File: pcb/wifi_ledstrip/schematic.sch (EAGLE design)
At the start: 64 parts, among them IC1 STM32F10XCXT6, Q1 8MHz

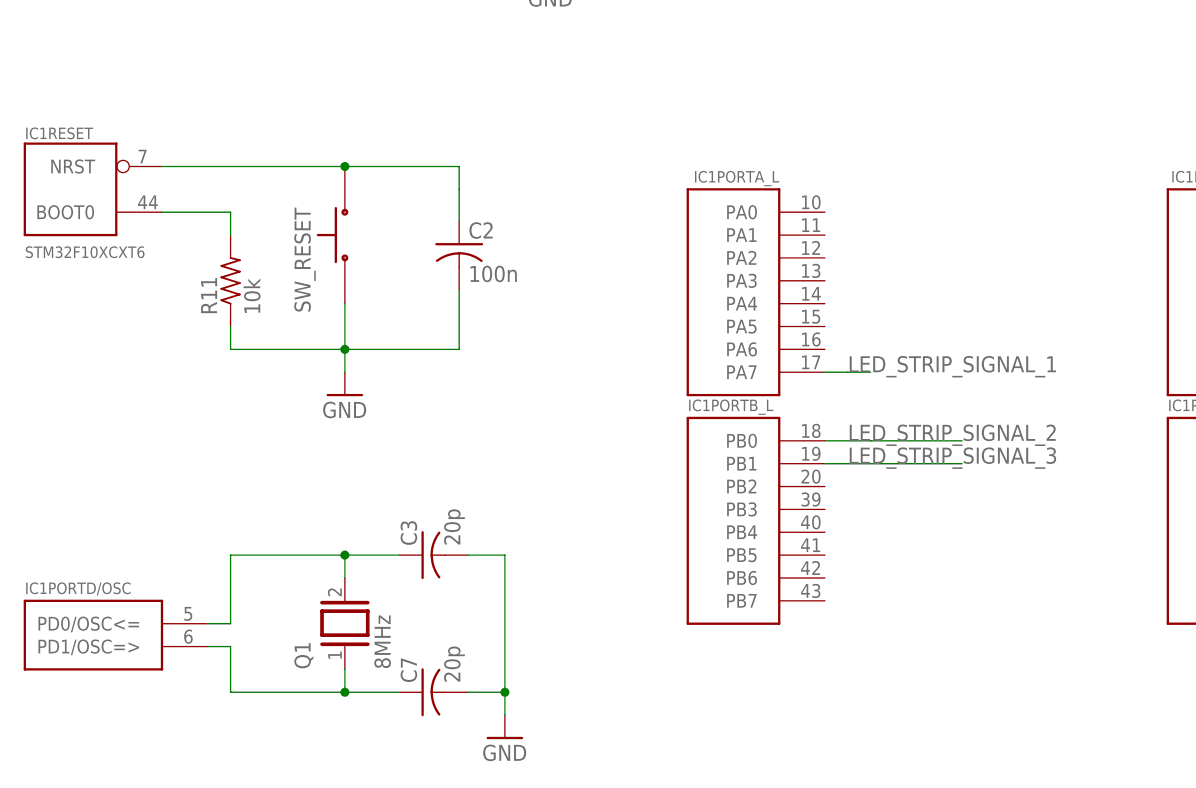
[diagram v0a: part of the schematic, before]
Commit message: pcb fix - boot1 pin pulled to gnd
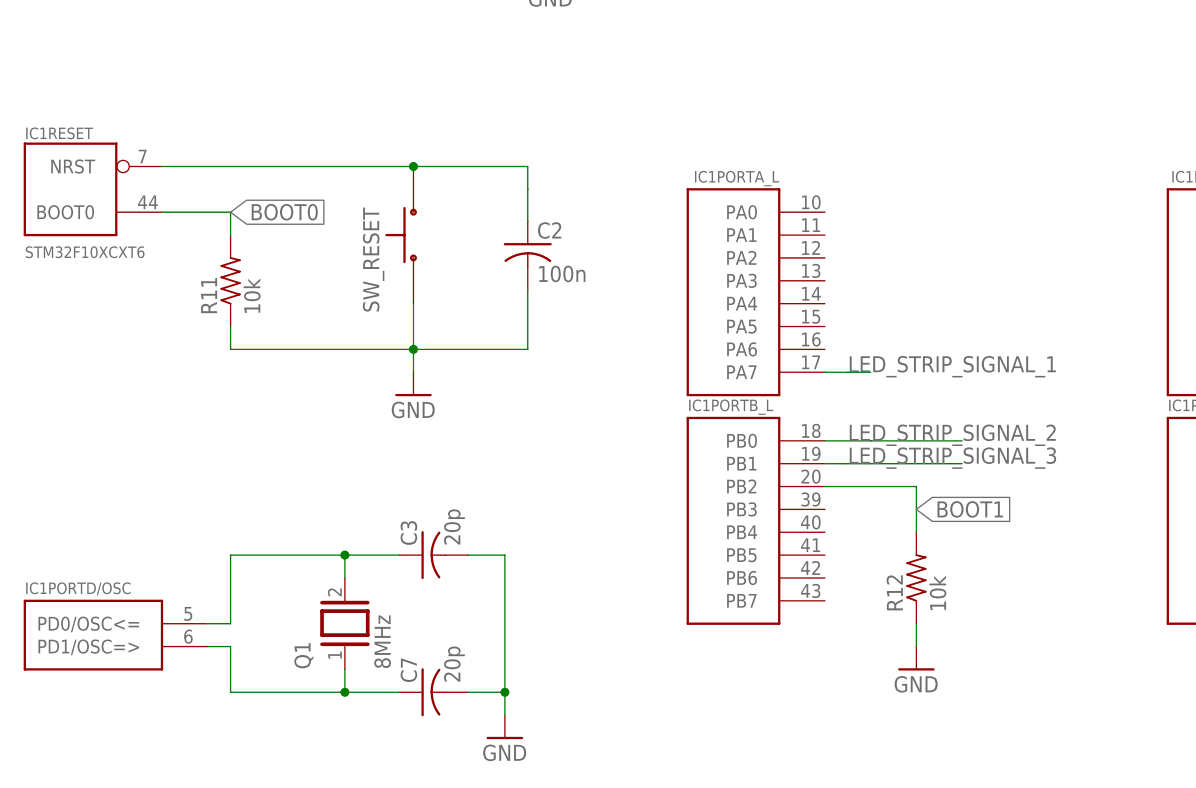
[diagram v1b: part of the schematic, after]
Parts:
- added R12: 10k, rcl:R-US_R1206
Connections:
- net N$16 renamed BOOT0
- new net BOOT1: IC1PORTB_L.PB2, R12.2
- net GND: now also R12.1
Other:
- moved on the sheet: C2, SW_RESET
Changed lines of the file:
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@@
 <?xml version="1.0" encoding="utf-8"?>
 <!DOCTYPE eagle SYSTEM "eagle.dtd">
-<eagle version="9.1.1">
+<eagle version="9.1.3">
 <drawing>
 <settings>
@@
 <part name="P+1" library="supply1" library_urn="urn:adsk.eagle:library:371" deviceset="+5V" device=""/>
 <part name="+3V8" library="supply1" library_urn="urn:adsk.eagle:library:371" deviceset="+3V3" device=""/>
+<part name="R12" library="rcl" library_urn="urn:adsk.eagle:library:334" deviceset="R-US_" device="R1206" package3d_urn="urn:adsk.eagle:package:23540/2" value="10k"/>
+<part name="GND17" library="supply1" library_urn="urn:adsk.eagle:library:371" deviceset="GND" device=""/>
 </parts>
 <sheets>
@@
 <instance part="LED_STRIP_12V" gate="J$1" x="149.86" y="66.04" rot="MR0"/>
 <instance part="LED_STRIP_GND" gate="J$1" x="134.62" y="50.8"/>
-<instance part="SW_RESET" gate="&gt;NAME" x="114.3" y="-38.1" rot="MR270"/>
+<instance part="SW_RESET" gate="&gt;NAME" x="121.92" y="-38.1" rot="MR270"/>
 <instance part="WIFI_RECONNECT" gate="&gt;NAME" x="30.48" y="17.78"/>
 <instance part="SW_3" gate="&gt;NAME" x="30.48" y="10.16"/>
@@
 <instance part="GND11" gate="1" x="205.74" y="-7.62"/>
 <instance part="GND12" gate="1" x="185.42" y="27.94"/>
-<instance part="GND13" gate="1" x="114.3" y="-55.88"/>
-<instance part="C2" gate="G$1" x="127" y="-39.116"/>
+<instance part="GND13" gate="1" x="121.92" y="-55.88"/>
+<instance part="C2" gate="G$1" x="134.62" y="-39.116"/>
 <instance part="C_VDD3" gate="G$1" x="45.72" y="-48.26"/>
 <instance part="C4" gate="G$1" x="38.1" y="-48.26"/>
@@
 <instance part="P+1" gate="1" x="190.5" y="91.44"/>
 <instance part="+3V8" gate="G$1" x="190.5" y="55.88"/>
+<instance part="R12" gate="G$1" x="177.8" y="-76.2" rot="R90"/>
+<instance part="GND17" gate="1" x="177.8" y="-86.36"/>
 </instances>
 <busses>
@@
 <segment>
 <pinref part="SW_RESET" gate="&gt;NAME" pin="P$4"/>
-<wire x1="114.3" y1="-45.72" x2="114.3" y2="-50.8" width="0.1524" layer="91"/>
+<wire x1="121.92" y1="-45.72" x2="121.92" y2="-50.8" width="0.1524" layer="91"/>
 <pinref part="GND13" gate="1" pin="GND"/>
 <pinref part="C2" gate="G$1" pin="2"/>
-<wire x1="114.3" y1="-50.8" x2="114.3" y2="-53.34" width="0.1524" layer="91"/>
-<wire x1="127" y1="-44.196" x2="127" y2="-50.8" width="0.1524" layer="91"/>
-<wire x1="127" y1="-50.8" x2="114.3" y2="-50.8" width="0.1524" layer="91"/>
-<junction x="114.3" y="-50.8"/>
+<wire x1="121.92" y1="-50.8" x2="121.92" y2="-53.34" width="0.1524" layer="91"/>
+<wire x1="134.62" y1="-44.196" x2="134.62" y2="-50.8" width="0.1524" layer="91"/>
+<wire x1="134.62" y1="-50.8" x2="121.92" y2="-50.8" width="0.1524" layer="91"/>
+<junction x="121.92" y="-50.8"/>
 <pinref part="R11" gate="G$1" pin="1"/>
 <wire x1="101.6" y1="-48.26" x2="101.6" y2="-50.8" width="0.1524" layer="91"/>
-<wire x1="101.6" y1="-50.8" x2="114.3" y2="-50.8" width="0.1524" layer="91"/>
+<wire x1="101.6" y1="-50.8" x2="121.92" y2="-50.8" width="0.1524" layer="91"/>
 </segment>
 <segment>
@@
 <junction x="340.36" y="-15.24"/>
 </segment>
+<segment>
+<pinref part="R12" gate="G$1" pin="1"/>
+<pinref part="GND17" gate="1" pin="GND"/>
+<wire x1="177.8" y1="-81.28" x2="177.8" y2="-83.82" width="0.1524" layer="91"/>
+</segment>
 </net>
 <net name="LED_STRIP_SIGNAL_1" class="0">
@@
 <segment>
 <pinref part="IC1" gate="RESET" pin="NRST"/>
-<wire x1="93.98" y1="-30.48" x2="114.3" y2="-30.48" width="0.1524" layer="91"/>
+<wire x1="93.98" y1="-30.48" x2="121.92" y2="-30.48" width="0.1524" layer="91"/>
 <pinref part="SW_RESET" gate="&gt;NAME" pin="P$3"/>
-<wire x1="114.3" y1="-30.48" x2="127" y2="-30.48" width="0.1524" layer="91"/>
-<junction x="114.3" y="-30.48"/>
-<wire x1="127" y1="-30.48" x2="127" y2="-33.02" width="0.1524" layer="91"/>
+<wire x1="121.92" y1="-30.48" x2="134.62" y2="-30.48" width="0.1524" layer="91"/>
+<junction x="121.92" y="-30.48"/>
+<wire x1="134.62" y1="-30.48" x2="134.62" y2="-33.02" width="0.1524" layer="91"/>
 <pinref part="C2" gate="G$1" pin="1"/>
-<wire x1="127" y1="-33.02" x2="127" y2="-36.576" width="0.1524" layer="91"/>
+<wire x1="134.62" y1="-33.02" x2="134.62" y2="-36.576" width="0.1524" layer="91"/>
 </segment>
 </net>
@@
 </segment>
 </net>
-<net name="N$16" class="0">
+<net name="BOOT0" class="0">
 <segment>
 <pinref part="IC1" gate="RESET" pin="BOOT0"/>
@@
 <pinref part="R11" gate="G$1" pin="2"/>
 <wire x1="101.6" y1="-35.56" x2="101.6" y2="-38.1" width="0.1524" layer="91"/>
+<label x="101.6" y="-35.56" size="1.778" layer="95" xref="yes"/>
 </segment>
 </net>
@@
 </segment>
 </net>
+<net name="BOOT1" class="0">
+<segment>
+<pinref part="IC1" gate="PORTB_L" pin="PB2"/>
+<pinref part="R12" gate="G$1" pin="2"/>
+<wire x1="167.64" y1="-66.04" x2="177.8" y2="-66.04" width="0.1524" layer="91"/>
+<wire x1="177.8" y1="-66.04" x2="177.8" y2="-71.12" width="0.1524" layer="91"/>
+<label x="177.8" y="-68.58" size="1.778" layer="95" xref="yes"/>
+</segment>
+</net>

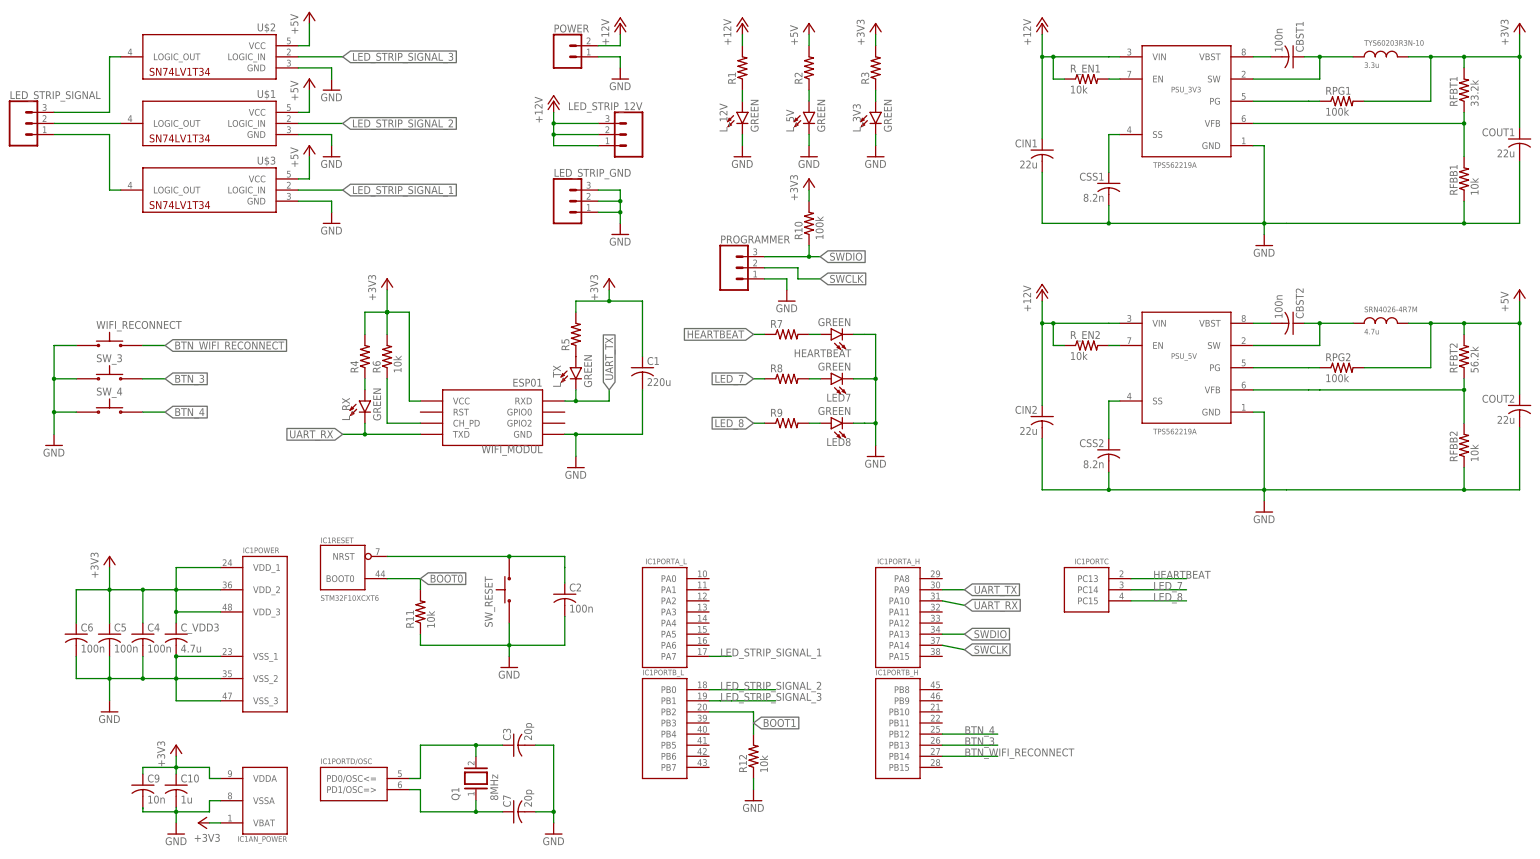
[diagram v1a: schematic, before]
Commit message: pcb fixed - 2 wires were mixed up - bigger capacitance to SS pin
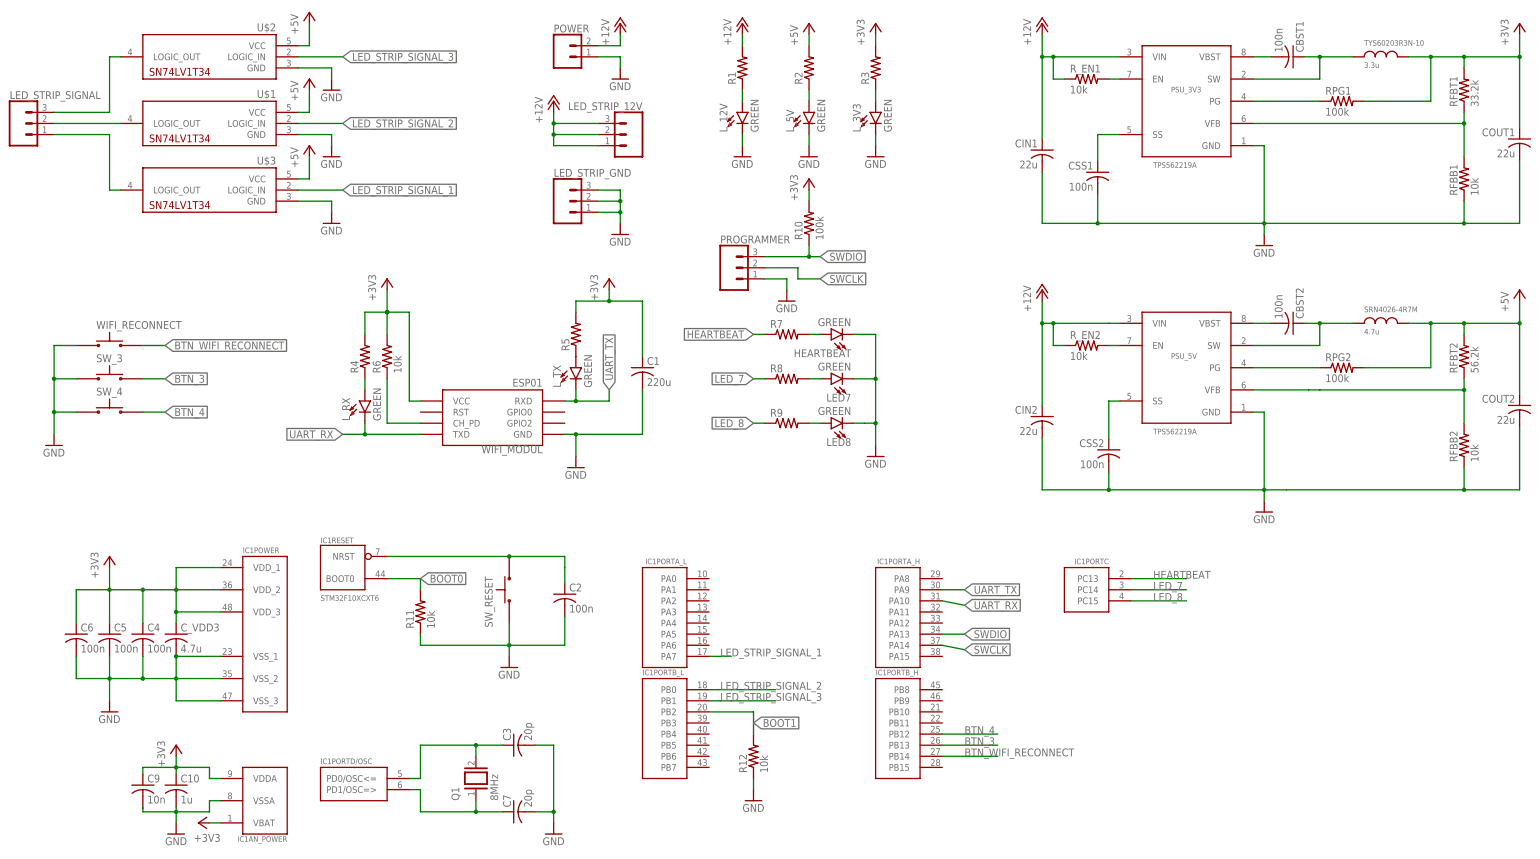
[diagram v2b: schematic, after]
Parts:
- CSS1, CSS2: value 8.2n -> 100n
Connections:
- net N$25 renamed N$SS1
- net N$28 renamed N$PG1
- net N$30 renamed N$SS2
- net N$34 renamed N$PG2
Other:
- moved on the sheet: CSS1
